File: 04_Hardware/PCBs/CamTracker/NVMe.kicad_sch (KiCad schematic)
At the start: 4 parts, among them J28 1-2199230-4, U7 PI3USB4000DZUAEX, U8 AP22655QWU-7, U9 PI3USB4000DZUAEX

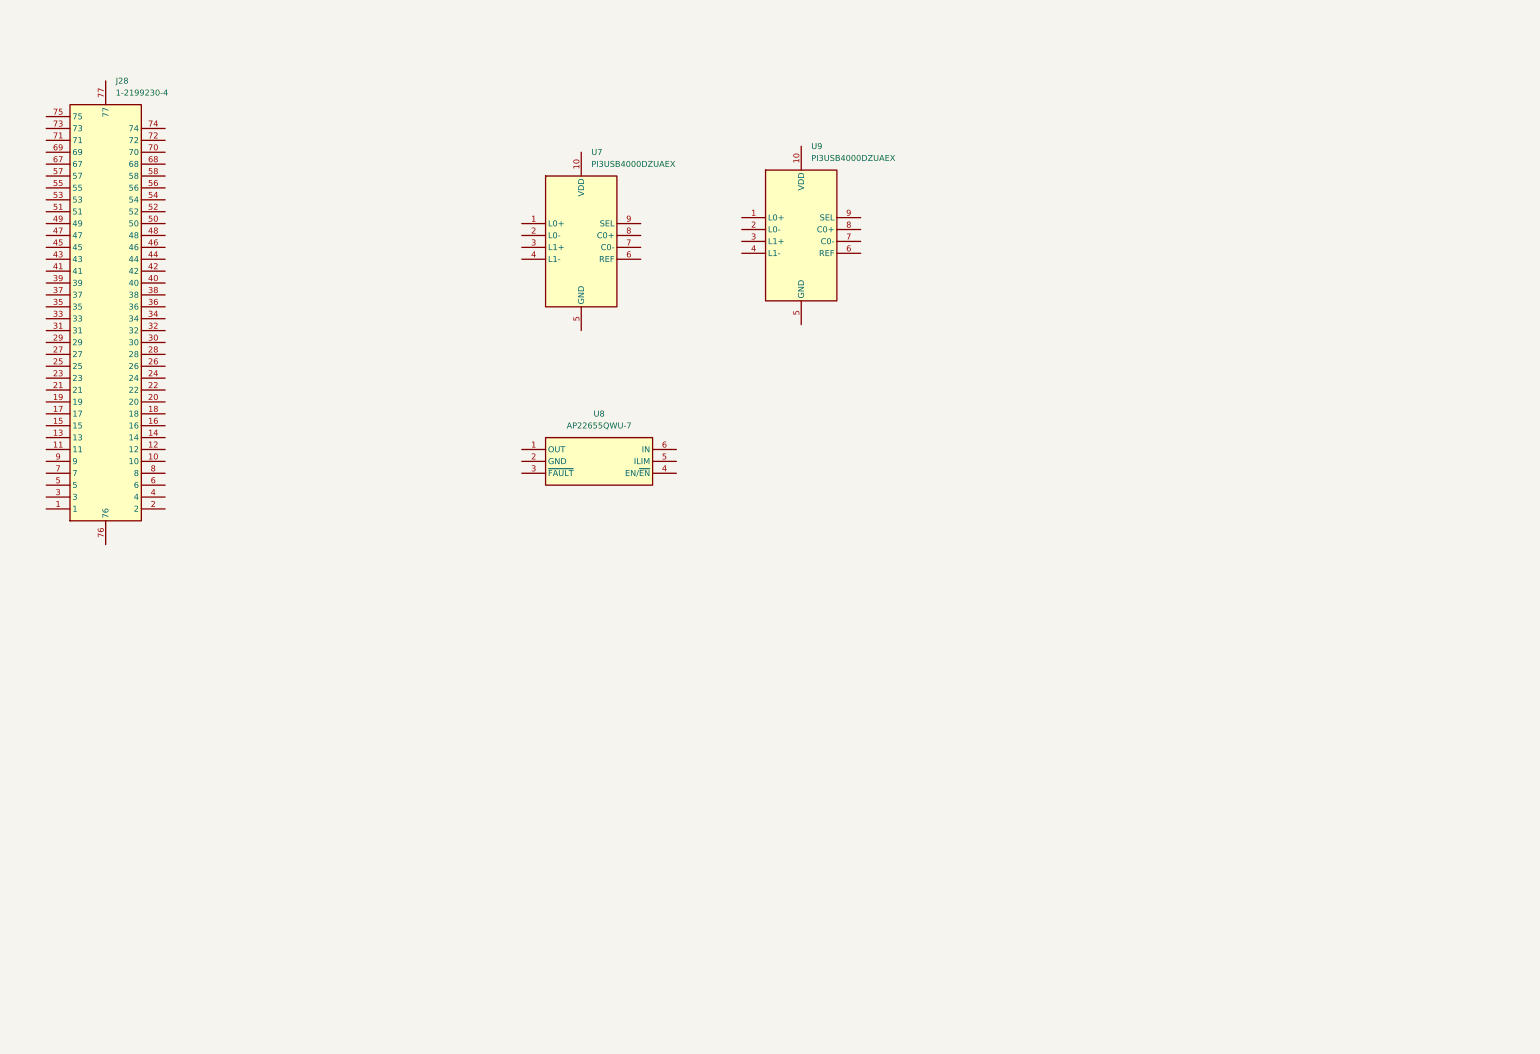
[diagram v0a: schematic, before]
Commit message: feat: Completed Placement v1 in Layout
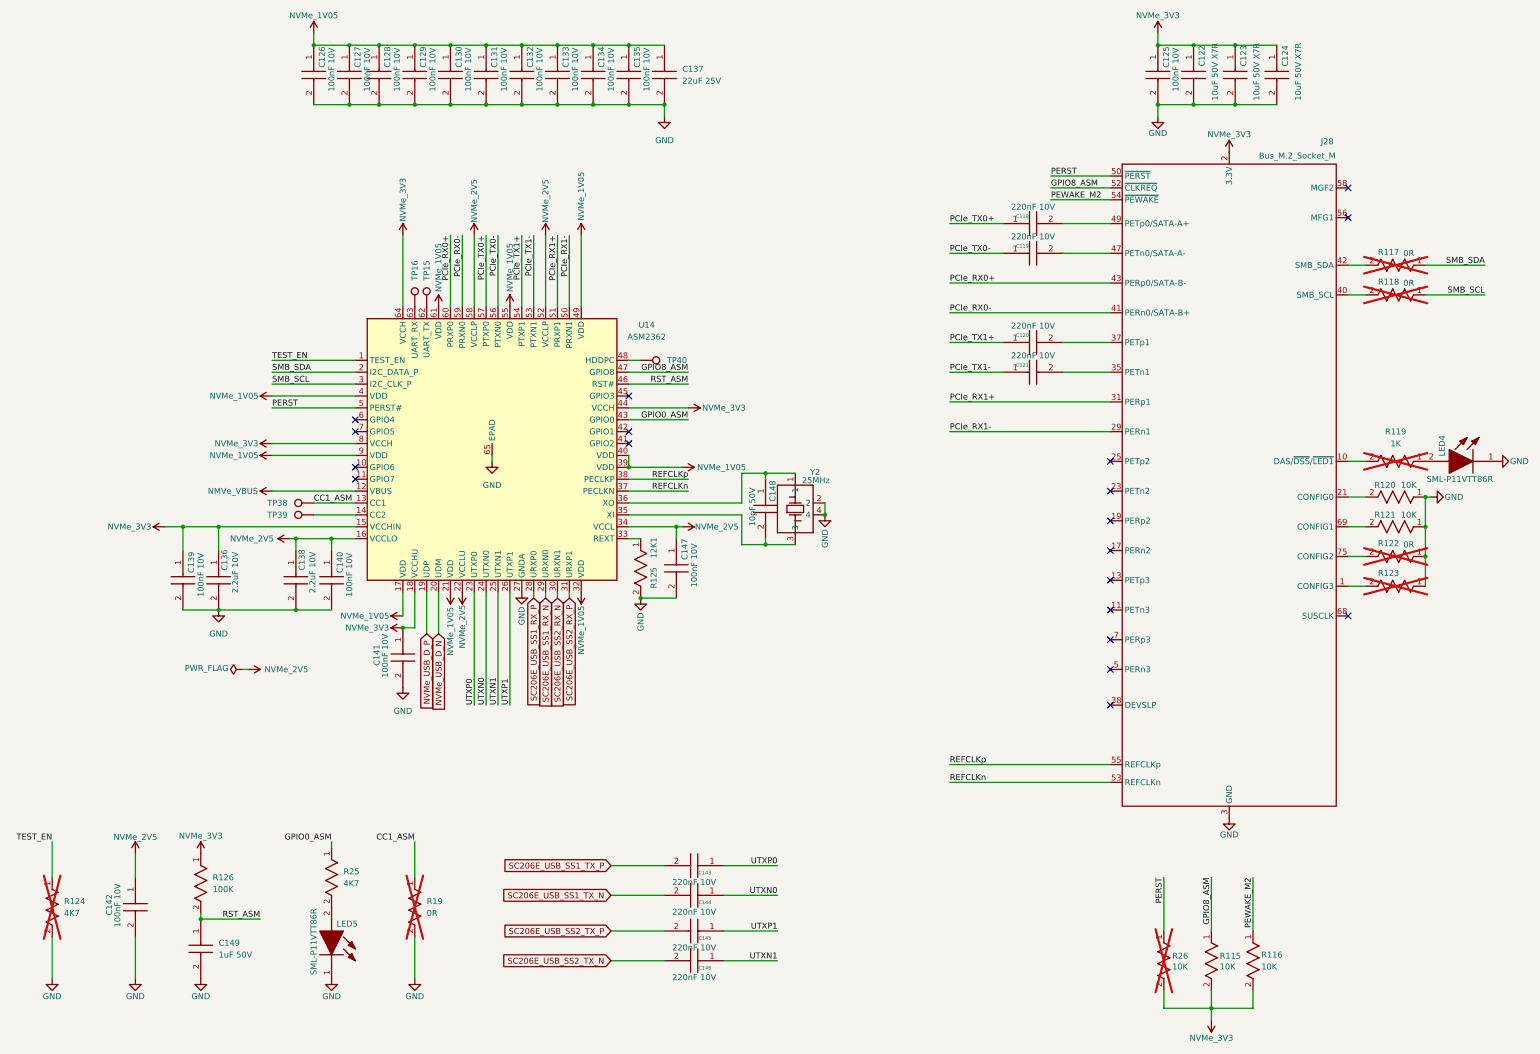
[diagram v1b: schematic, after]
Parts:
- removed J28: 1-2199230-4, 000MCLib:121992304, symbol 000MCLib:1-2199230-4
- removed U7, U9: PI3USB4000DZUAEX, 000MCLib:PI3USB4000DZUAEX, symbol 000MCLib:PI3USB4000DZUAEX
- removed U8: AP22655QWU-7, 000MCLib:SOT95P280X82-6N, symbol 000MCLib:AP22655QWU-7
- added C118, C119, C120, C121, C143, C144, C145, C146: 220nF 10V, 000MCLib:CAPC1005X55N, symbol 000MCLib:GRM155R61A224JE19D
- added C122, C123, C124: 10uF 50V X7R, 000MCLib:CAPC3216X190N, symbol 000MCLib:CL31B106KBK6PJE
- added C125, C126, C127, C128, C129, C130, C131, C132, C133, C134, C135, C139, C140, C141, C142, C147: 100nF 10V, 000MCLib:CAPC1005X55N, symbol 000MCLib:GRM155R71A104KA01D
- added C136, C138: 2.2uF 10V, 000MCLib:CAPC1608X90N, symbol 000MCLib:LMK107BJ225KA-T
- added C137: 22uF 25V, 000MCLib:CAPC2012X145N, symbol 000MCLib:GRM21BR61E226ME44L
- added C148: 10pF 50V, 000MCLib:CAPC1005X55N, symbol 000MCLib:GRM1555C1H100JA01D
- added C149: 1uF 50V, 000MCLib:CAPC1005X55N, symbol 000MCLib:GRM155R61H105KE05D
- added J28: Bus_M.2_Socket_M, 000MCLib:121992304, symbol 000MCLib:Bus_M.2_Socket_M
- added LED4, LED5: SML-P11VTT86R, 000MCLib:SMLP11VTT86R, symbol 000MCLib:SML-P11VTT86R
- added R115, R116, R120, R121, R26: 10K, 000MCLib:RC0402N_YAG, symbol 000MCLib:RC0402JR-0710KL
- added R117, R118, R122, R123: 0R, 000MCLib:RC0402N_YAG, symbol 000MCLib:RC0402JR-070RL
- added R119: 1K, 000MCLib:RC0402N_YAG, symbol 000MCLib:RC0402JR-071KL
- added R124, R25: 4K7, 000MCLib:RC0402N_YAG, symbol 000MCLib:RC0402JR-074K7L
- added R125: 12K1, 000MCLib:RC0402N_YAG, symbol 000MCLib:RT1206FRE0712K1L
- added R126: 100K, 000MCLib:RC0402N_YAG, symbol 000MCLib:RC0402JR-07100KL
- added R19: 0R, 000MCLib:RESC2012X50N, symbol 000MCLib:CRCW08050000Z0EA
- added TP15, TP16, TP38, TP39, TP40: 3.86V, TestPoint:TestPoint_Pad_D1.0mm, symbol 000MCLib:TestPoint
- added U14: ASM2362, 000MCLib:QFN50P905X905X75-65N, symbol 000MCLib:ASM2362
- added Y2: 25MHz, 000MCLib:FL2500188, symbol 000MCLib:FL2500188
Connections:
- new net: J28.21 (CONFIG0), R120.2
- new net: C148.1, U14.36 (XO), Y2.1
- new net: C148.2, U14.35 (XI), Y2.3
- new net: J28.1 (CONFIG3), R123.2
- new net: J28.10 (DAS/~{DSS}/~{LED1}), R119.2
- new net: C121.2, J28.35 (PETn1)
- new net: C120.2, J28.37 (PETp1)
- new net: J28.40 (SMB_SCL), R118.2
- new net: J28.42 (SMB_SDA), R117.2
- new net: C119.2, J28.47 (PETn0/SATA-A-)
- new net: C118.2, J28.49 (PETp0/SATA-A+)
- new net: J28.69 (CONFIG1), R121.2
- new net: J28.75 (CONFIG2), R122.2
- new net: TP40.1, U14.48 (HDDPC)
- new net: LED4.2 (A), R119.1
- new net: R125.1, U14.33 (REXT)
- new net: LED5.2 (A), R25.2
- new net: TP39.1, U14.14 (CC2)
- new net: TP15.1, U14.62 (UART_TX)
- new net: TP16.1, U14.63 (UART_RX)
- new net 3.3V: C122.1, C123.1, C124.1, C125.1, C136.1, C139.1, C141.1, J28.12 (3.3V), J28.14 (3.3V), J28.16 (3.3V), J28.18 (3.3V), J28.2 (3.3V), J28.4 (3.3V), J28.70 (3.3V), J28.72 (3.3V), J28.74 (3.3V), R115.2, R116.2, R126.1, R26.2, U14.15 (VCCHIN), U14.18 (VCCHU), U14.44 (VCCH), U14.64 (VCCH), U14.8 (VCCH)
- new net CC1_ASM: R19.1, TP38.1, U14.13 (CC1)
- new net GND: C122.2, C123.2, C124.2, C125.2, C126.2, C127.2, C128.2, C129.2, C130.2, C131.2, C132.2, C133.2, C134.2, C135.2, C136.2, C137.2, C138.2, C139.2, C140.2, C141.2, C142.2, C147.2, C149.2, J28.15 (GND), J28.27 (GND), J28.3 (GND), J28.33 (GND), J28.39 (GND), J28.45 (GND), J28.51 (GND), J28.57 (GND), J28.71 (GND), J28.73 (GND), J28.76 (GND), J28.77 (GND), J28.9 (GND), LED4.1 (K), LED5.1 (K), R120.1, R121.1, R122.1, R123.1, R124.2, R125.2, R19.2, U14.27 (GNDA), U14.65 (EPAD), Y2.2, Y2.4
- new net GPIO0_ASM: R25.1, U14.43 (GPIO0)
- new net GPIO8_ASM: J28.52 (~{CLKREQ}), R115.1, U14.47 (GPIO8)
- new net NMVe_VBUS: U14.12 (VBUS)
- new net NVMe_1V05: C126.1, C127.1, C128.1, C129.1, C130.1, C131.1, C132.1, C133.1, C134.1, C135.1, C137.1, U14.17 (VDD), U14.21 (VDD), U14.32 (VDD), U14.39 (VDD), U14.4 (VDD), U14.40 (VDD), U14.49 (VDD), U14.55 (VDD), U14.61 (VDD), U14.9 (VDD)
- new net NVMe_2V5: C138.1, C140.1, C142.1, C147.1, U14.16 (VCCLO), U14.22 (VCCLU), U14.34 (VCCL), U14.52 (VCCLP), U14.58 (VCCLP)
- new net NVMe_USB_D_N: U14.20 (UDM)
- new net NVMe_USB_D_P: U14.19 (UDP)
- new net PCIe_RX0+: J28.43 (PERp0/SATA-B-), U14.60 (PRXP0)
- new net PCIe_RX0-: J28.41 (PERn0/SATA-B+), U14.59 (PRXN0)
- new net PCIe_RX1+: J28.31 (PERp1), U14.51 (PRXP1)
- new net PCIe_RX1-: J28.29 (PERn1), U14.50 (PRXN1)
- new net PCIe_TX0+: C118.1, U14.57 (PTXP0)
- new net PCIe_TX0-: C119.1, U14.56 (PTXN0)
- new net PCIe_TX1+: C120.1, U14.54 (PTXP1)
- new net PCIe_TX1-: C121.1, U14.53 (PTXN1)
- new net PERST: J28.50 (~{PERST}), R26.1, U14.5 (PERST#)
- new net PEWAKE_M2: J28.54 (~{PEWAKE}), R116.1
- new net REFCLKn: J28.53 (REFCLKn), U14.37 (PECLKN)
- new net REFCLKp: J28.55 (REFCLKp), U14.38 (PECLKP)
- new net RST_ASM: C149.1, R126.2, U14.46 (RST#)
- new net SC206E_USB_SS1_RX_N: U14.29 (URXN0)
- new net SC206E_USB_SS1_RX_P: U14.28 (URXP0)
- new net SC206E_USB_SS1_TX_N: C144.2
- new net SC206E_USB_SS1_TX_P: C143.2
- new net SC206E_USB_SS2_RX_N: U14.30 (URXN1)
- new net SC206E_USB_SS2_RX_P: U14.31 (URXP1)
- new net SC206E_USB_SS2_TX_N: C146.2
- new net SC206E_USB_SS2_TX_P: C145.2
- new net SMB_SCL: R118.1, U14.3 (I2C_CLK_P)
- new net SMB_SDA: R117.1, U14.2 (I2C_DATA_P)
- new net TEST_EN: R124.1, U14.1 (TEST_EN)
- new net UTXN0: C144.1, U14.24 (UTXN0)
- new net UTXN1: C146.1, U14.25 (UTXN1)
- new net UTXP0: C143.1, U14.23 (UTXP0)
- new net UTXP1: C145.1, U14.26 (UTXP1)
- no-connect marks 0 -> 19
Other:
- company: (none) -> Author: Mehmet Cihangir
- title: (none) -> NVMe SSD

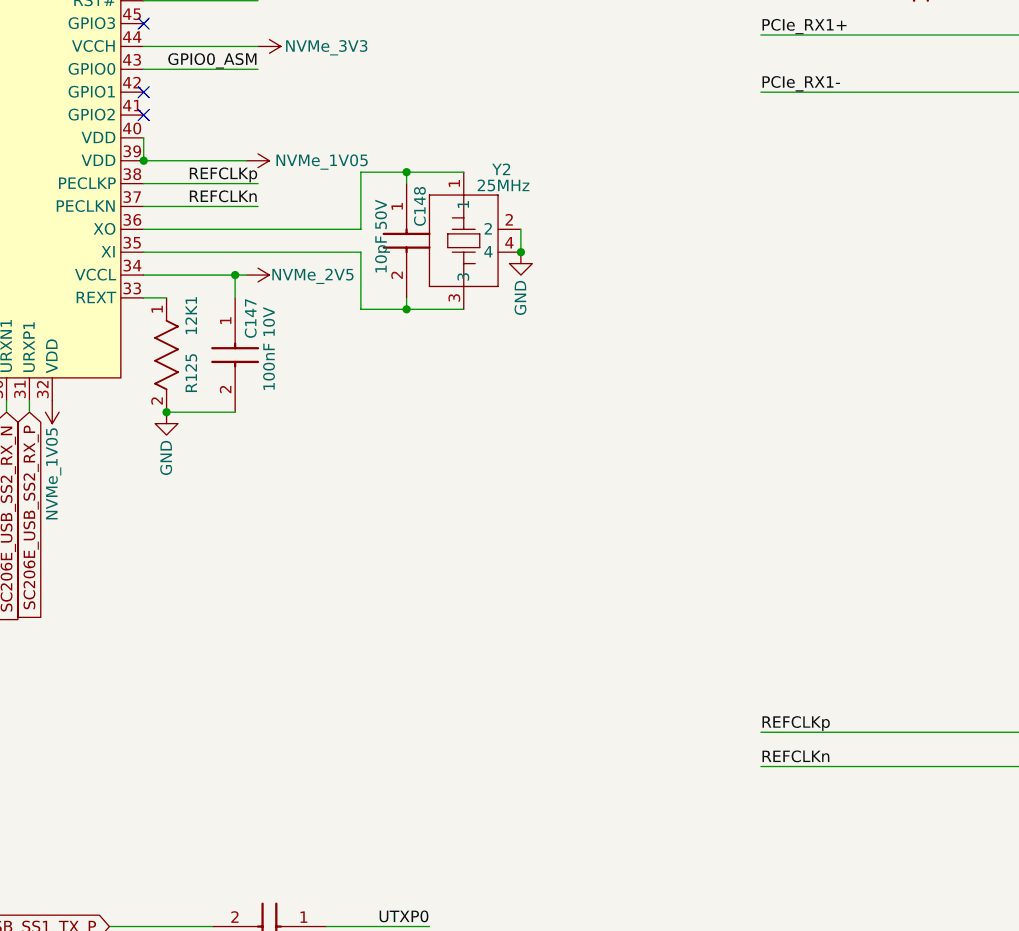
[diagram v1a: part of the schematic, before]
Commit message: feat(layout): Routed DP traces
Includes:
- Routed DP Camera/USB/PCIe
- Routed SIM/SD
- Routed ASM
- Routed RP
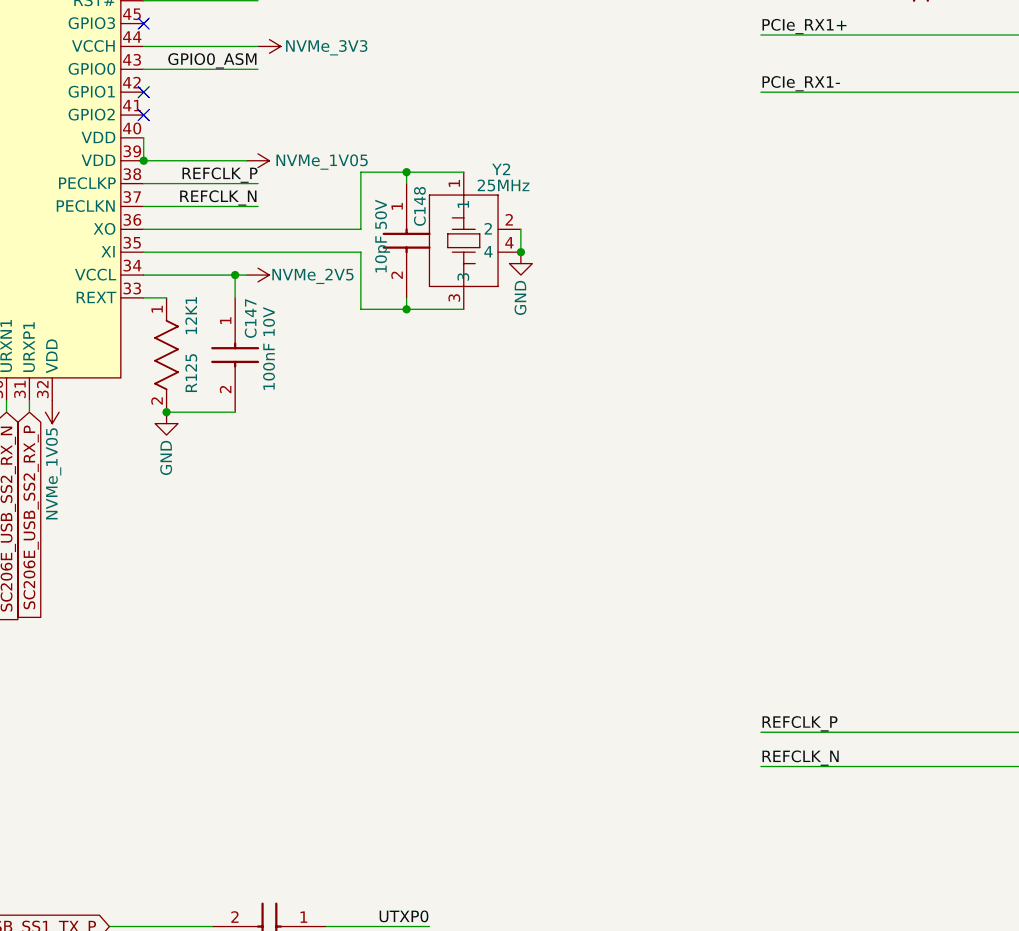
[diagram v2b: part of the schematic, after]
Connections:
- net REFCLKn renamed REFCLK_N
- net REFCLKp renamed REFCLK_P
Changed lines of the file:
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@@
 		)
 	)
-	(label "REFCLKn"
+	(label "REFCLK_N"
 		(at 175.26 125.73 180)
 		(effects
@@
 		)
 	)
-	(label "REFCLKp"
+	(label "REFCLK_P"
 		(at 231.14 184.15 0)
 		(effects
@@
 		)
 	)
-	(label "REFCLKn"
+	(label "REFCLK_N"
 		(at 231.14 187.96 0)
 		(effects
@@
 		)
 	)
-	(label "REFCLKp"
+	(label "REFCLK_P"
 		(at 175.26 123.19 180)
 		(effects

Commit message: feat(layout): Completed Layout Design with new Camera Connectors
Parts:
- J28: footprint 000MCLib:121992304 -> 000MCLib:NVMEE
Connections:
- net GND: now also J28.0 (GND)
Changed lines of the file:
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@@
+	(wire
+		(pts
+			(xy 316.23 146.05) (xy 320.04 146.05)
+		)
+		(stroke
+			(width 0)
+			(type default)
+		)
+	)
 	(wire
 		(pts
@@
 		(pts
 			(xy 162.56 120.65) (xy 173.99 120.65)
-		)
-		(stroke
-			(width 0)
-			(type default)
-		)
-	)
-	(wire
-		(pts
-			(xy 316.23 146.05) (xy 320.04 146.05)
 		)
 		(stroke
@@
 			)
 		)
-		(property "Footprint" "000MCLib:121992304"
+		(property "Footprint" "000MCLib:NVMEE"
 			(at 290.83 74.93 0)
 			(effects
@@
 		(pin "69"
 		)
+		(pin "0"
+		)
 		(instances

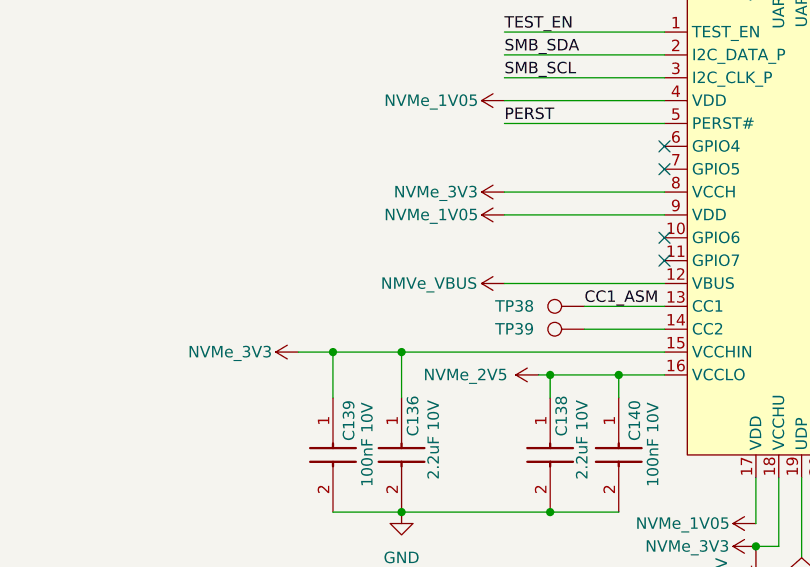
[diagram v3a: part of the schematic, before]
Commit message: feat(PCB): Finalized design and generated Gerber files and BOM
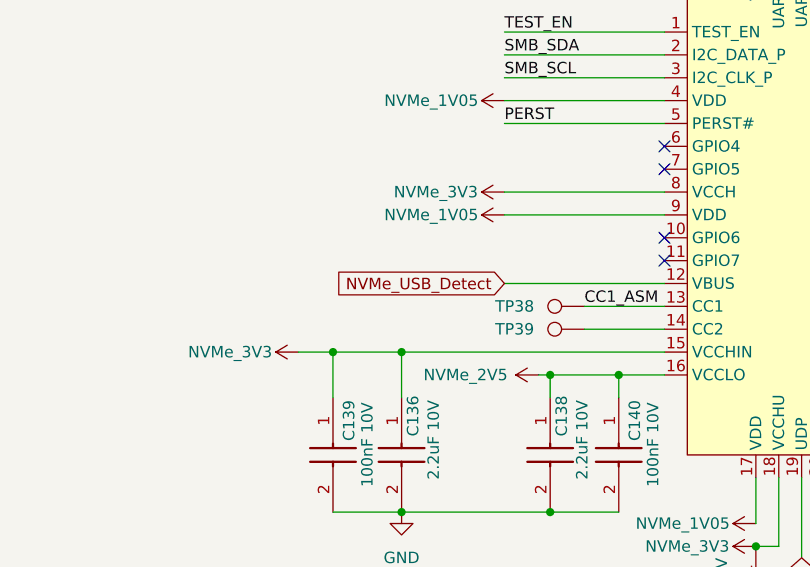
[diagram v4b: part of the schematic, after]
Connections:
- net NMVe_VBUS renamed NVMe_USB_Detect

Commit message: feat(PCB): finalize PCB design and generate BOM/Gerbers
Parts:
- R19: Height 0.5 -> (none); Mouser Part Number 71-CRCW0805-0-E3 -> (none); Mouser Price/Stock https://www.mouser.co.uk/ProductDetail/Vishay-Dale/CRCW0805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 -> (none)
